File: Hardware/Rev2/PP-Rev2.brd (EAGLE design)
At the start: 190.5 x 101.3 mm, 181 parts, among them IC1 LT6004, IC2 TLC6C5912-Q1, J1 J_0399700102, Q1 MOSFET-PCHANNEL, Q10 2N7002PW, Q11 2N7002PW, Q12 2N7002PW, Q13 2N7002PW, Q14 2N7002PW, Q15 2N7002PW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

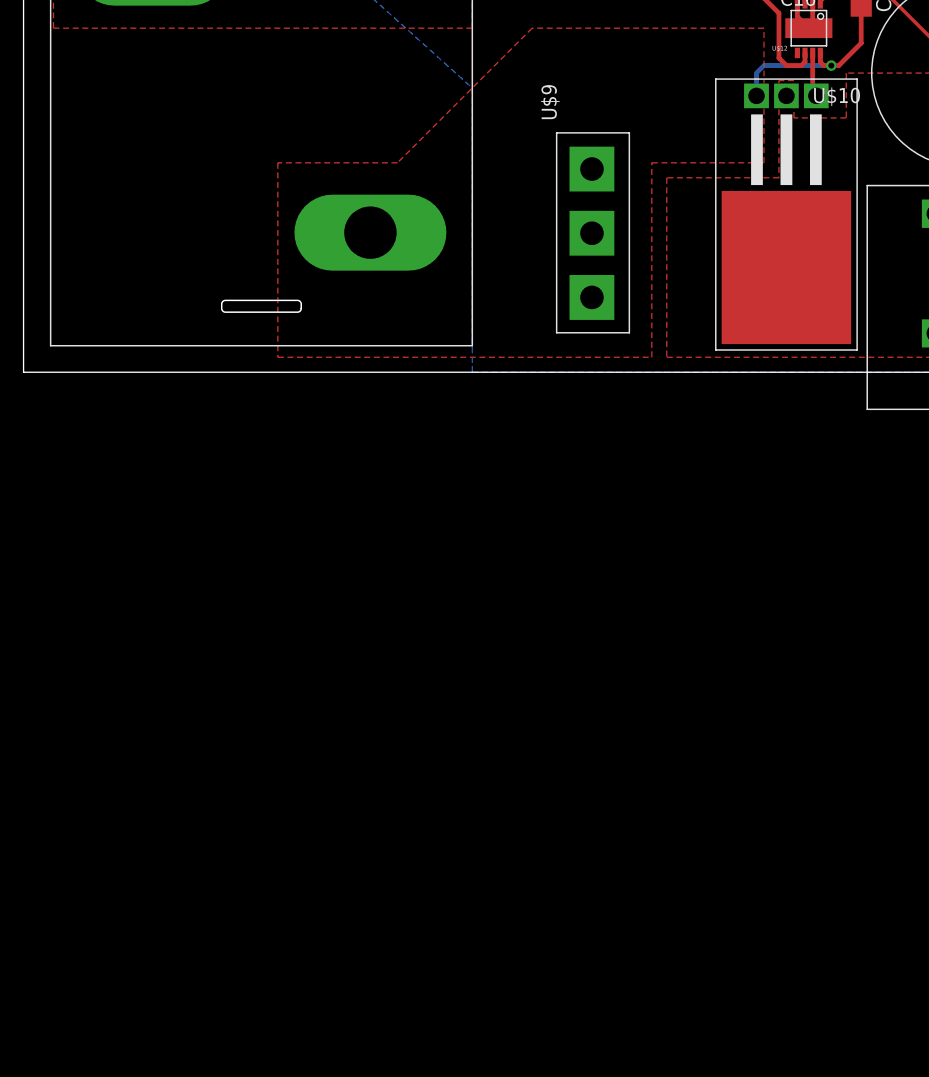
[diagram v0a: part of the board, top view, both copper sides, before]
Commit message: Changing out charger MOSFET to proper component
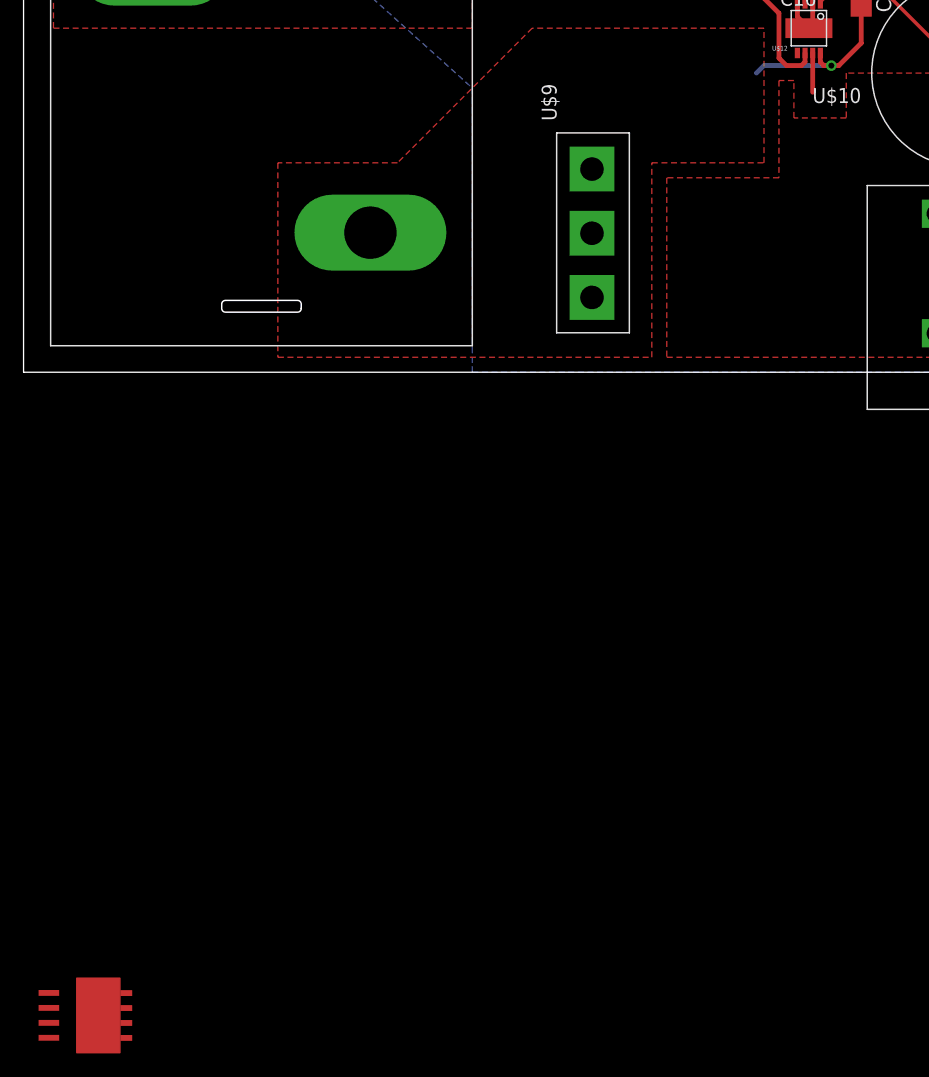
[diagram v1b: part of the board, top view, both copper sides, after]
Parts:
- removed Q9: CSD18532, PCB0M1:TO-220-FLAT
- added U$16: IRFH7191, 2016PowerPackLibraries:PQFN5X6B
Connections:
- net CHARGER+: now also U$16.P$5, U$16.P$6, U$16.P$7, U$16.P$8; no longer Q9.2, Q9.4
- net N$39: now also U$16.P$1, U$16.P$2, U$16.P$3; no longer Q9.3
- net N$40: now also U$16.P$4; no longer Q9.1
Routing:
- net N$39: track 16.8 -> 14.8 mm
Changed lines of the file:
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@@
 <?xml version="1.0" encoding="utf-8"?>
 <!DOCTYPE eagle SYSTEM "eagle.dtd">
-<eagle version="7.1.0">
+<eagle version="6.5.0">
 <drawing>
 <settings>
@@
 <pass name="Default">
 <param name="RoutingGrid" value="50mil"/>
-<param name="AutoGrid" value="1"/>
-<param name="Efforts" value="0"/>
-<param name="TopRouterVariant" value="1"/>
 <param name="tpViaShape" value="round"/>
 <param name="PrefDir.1" value="|"/>
@@
 <element name="U$7" library="MRDT-2015-PowerBoard" package="C_16MM" value="C_108CKH050M" x="11.43" y="54.61"/>
 <element name="U$9" library="2016PowerPackLibraries" package="TO-247-VERT" value="D-STTH60P03SW" x="48.26" y="6.35" rot="R90"/>
-<element name="Q9" library="PCB0M1" package="TO-220-FLAT" value="CSD18532" x="64.77" y="8.89" rot="R180"/>
 <element name="U$10" library="MRDT-2015-PowerBoard" package="C_16MM" value="C_108CKH050M" x="80.01" y="25.4" rot="R180"/>
 <element name="U$11" library="MRDT-2015-PowerBoard" package="C_16MM" value="C_108CKH050M" x="97.79" y="27.305" rot="R180"/>
@@
 <element name="U$15" library="MAX3077" package="MAX3070E" value="MAX3077" x="179.705" y="47.625"/>
 <element name="J1" library="MRDT-2014-All" package="J_2CONHC" value="J_0399700102" x="82.55" y="6.35"/>
+<element name="U$16" library="2016PowerPackLibraries" package="PQFN5X6B" value="IRFH7191" x="6.35" y="-54.61"/>
 </elements>
 <signals>
@@
 </signal>
 <signal name="CHARGER+">
-<contactref element="Q9" pad="4"/>
-<contactref element="Q9" pad="2"/>
 <contactref element="U$10" pad="+"/>
 <contactref element="U$11" pad="+"/>
@@
 <wire x1="100.33" y1="21.59" x2="97.85" y2="21.59" width="0.3048" layer="16"/>
 <wire x1="97.85" y1="21.59" x2="97.79" y2="23.555" width="0.3048" layer="16"/>
+<contactref element="U$16" pad="P$5"/>
+<contactref element="U$16" pad="P$6"/>
+<contactref element="U$16" pad="P$7"/>
+<contactref element="U$16" pad="P$8"/>
+<wire x1="80.01" y1="21.65" x2="97.85" y2="21.59" width="0" layer="19" extent="16-16"/>
+<wire x1="77.47" y1="13.46" x2="80.01" y2="21.65" width="0" layer="19" extent="1-1"/>
+<wire x1="77.47" y1="3.3" x2="77.47" y2="13.46" width="0" layer="19" extent="1-1"/>
+<wire x1="8.725" y1="-52.71" x2="77.47" y2="3.3" width="0" layer="19" extent="1-1"/>
+<wire x1="8.725" y1="-53.98" x2="8.725" y2="-52.71" width="0" layer="19" extent="1-1"/>
+<wire x1="8.725" y1="-55.25" x2="8.725" y2="-53.98" width="0" layer="19" extent="1-1"/>
+<wire x1="8.725" y1="-56.52" x2="8.725" y2="-55.25" width="0" layer="19" extent="1-1"/>
 </signal>
 <signal name="V_CHECK_CHARGER_IN">
@@
 <contactref element="U$5" pad="P$2"/>
 <contactref element="U$9" pad="P$2"/>
-<contactref element="Q9" pad="3"/>
 <polygon width="1.016" layer="1" thermals="no">
 <vertex x="62.865" y="17.78"/>
@@
 <wire x1="68.58" y1="26.035" x2="62.865" y2="26.035" width="0.4064" layer="16"/>
 <wire x1="62.865" y1="26.035" x2="62.23" y2="25.4" width="0.4064" layer="16"/>
-<wire x1="62.23" y1="25.4" x2="62.23" y2="23.46" width="0.4064" layer="16"/>
+<contactref element="U$16" pad="P$1"/>
+<contactref element="U$16" pad="P$2"/>
+<contactref element="U$16" pad="P$3"/>
+<wire x1="48.26" y1="11.8" x2="62.23" y2="25.4" width="0" layer="19" extent="16-16"/>
+<wire x1="29.45" y1="11.85" x2="48.26" y2="11.8" width="0" layer="19" extent="1-1"/>
+<wire x1="2.15" y1="-52.7" x2="29.45" y2="11.85" width="0" layer="19" extent="1-1"/>
+<wire x1="2.15" y1="-53.97" x2="2.15" y2="-52.7" width="0" layer="19" extent="1-1"/>
+<wire x1="2.15" y1="-55.24" x2="2.15" y2="-53.97" width="0" layer="19" extent="1-1"/>
 </signal>
 <signal name="N$40">
 <contactref element="U$12" pad="P$7"/>
-<contactref element="Q9" pad="1"/>
 <wire x1="67" y1="27.1045" x2="67" y2="23.77" width="0.4064" layer="1"/>
-<wire x1="67" y1="23.77" x2="67.31" y2="23.46" width="0.4064" layer="1"/>
+<contactref element="U$16" pad="P$4"/>
+<wire x1="2.15" y1="-56.51" x2="67" y2="23.77" width="0" layer="19" extent="1-1"/>
 </signal>
 <signal name="CHARGER_CTL">

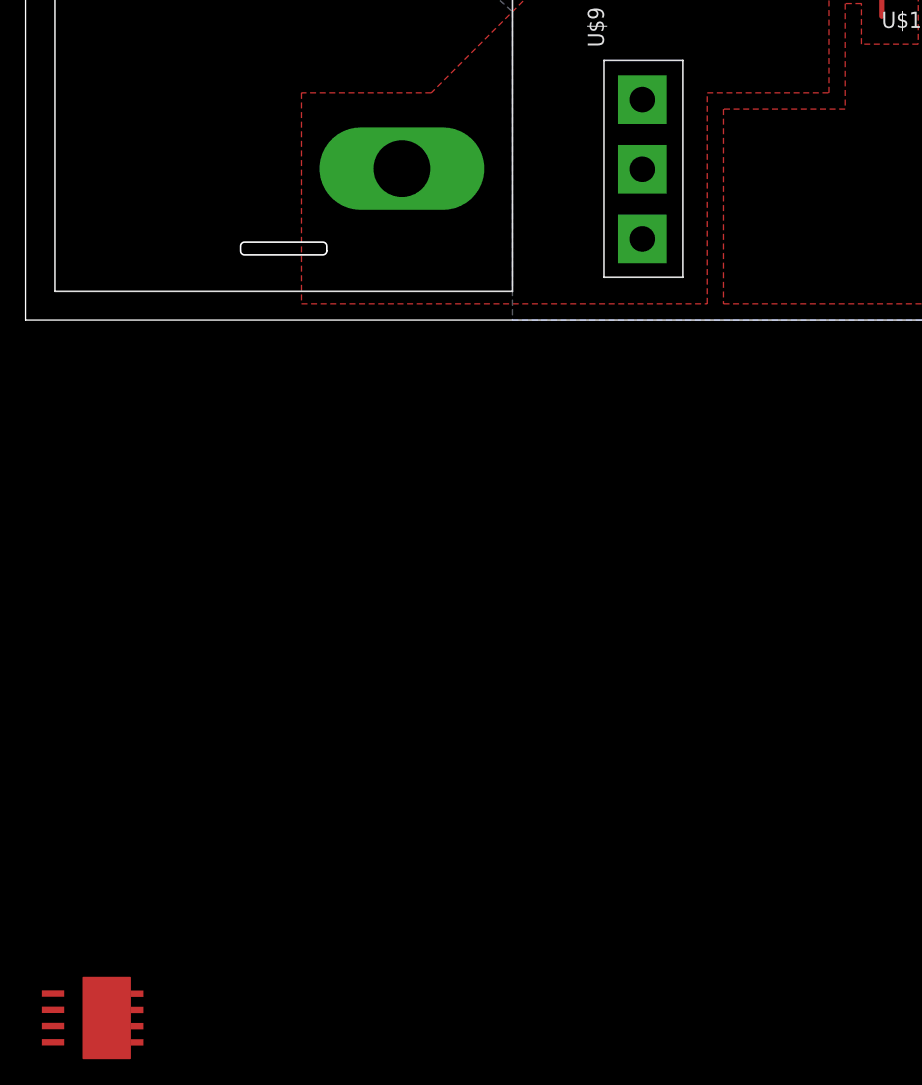
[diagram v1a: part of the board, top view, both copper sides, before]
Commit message: Complete SPICE sim for 90% duty cycle case. Updated Eagle files with proper MOSFET
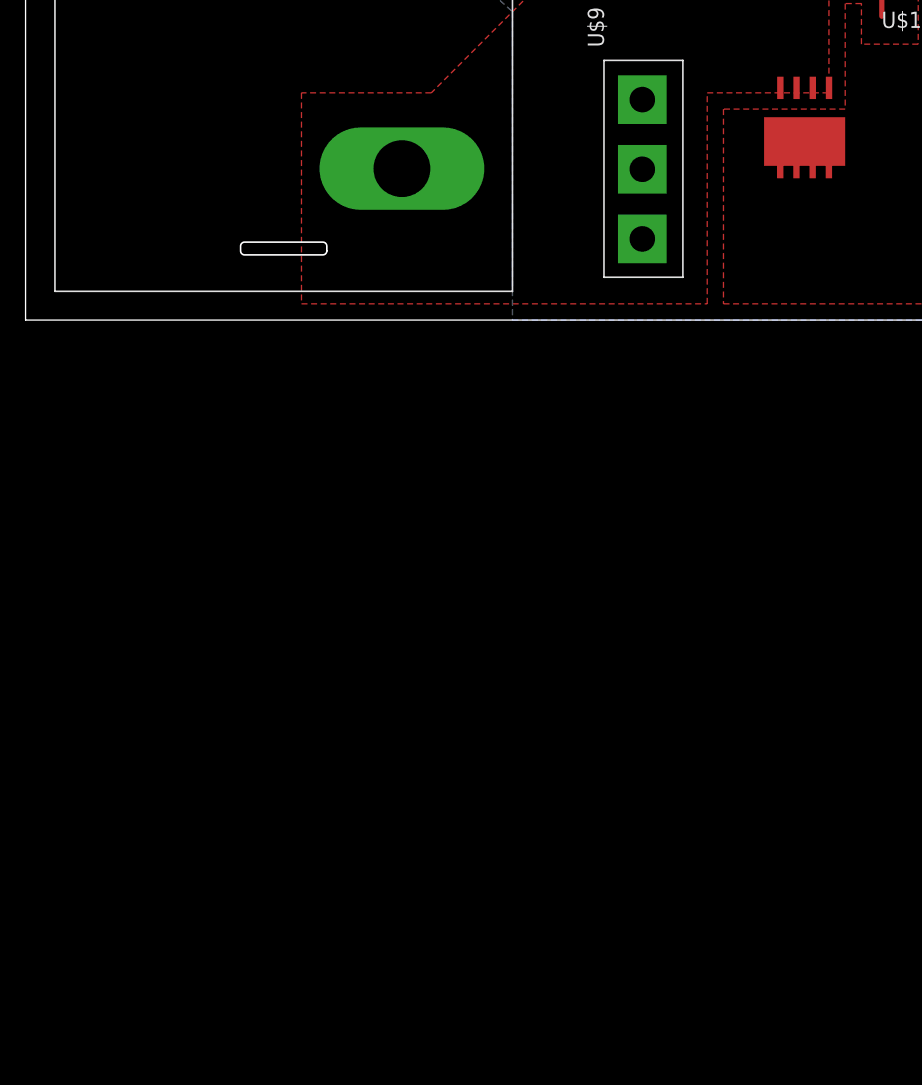
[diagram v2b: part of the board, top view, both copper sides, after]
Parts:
- moved U$16 87.7 mm to (61.0, 14.0), turned to 270 degrees
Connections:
- net CHARGER+: now also U$16.P$9
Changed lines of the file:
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@@
 <element name="U$15" library="MAX3077" package="MAX3070E" value="MAX3077" x="179.705" y="47.625"/>
 <element name="J1" library="MRDT-2014-All" package="J_2CONHC" value="J_0399700102" x="82.55" y="6.35"/>
-<element name="U$16" library="2016PowerPackLibraries" package="PQFN5X6B" value="IRFH7191" x="6.35" y="-54.61"/>
+<element name="U$16" library="2016PowerPackLibraries" package="PQFN5X6B" value="IRFH7191" x="60.96" y="13.97" rot="R270"/>
 </elements>
 <signals>
@@
 <contactref element="U$16" pad="P$7"/>
 <contactref element="U$16" pad="P$8"/>
-<wire x1="80.01" y1="21.65" x2="97.85" y2="21.59" width="0" layer="19" extent="16-16"/>
-<wire x1="77.47" y1="13.46" x2="80.01" y2="21.65" width="0" layer="19" extent="1-1"/>
-<wire x1="77.47" y1="3.3" x2="77.47" y2="13.46" width="0" layer="19" extent="1-1"/>
-<wire x1="8.725" y1="-52.71" x2="77.47" y2="3.3" width="0" layer="19" extent="1-1"/>
-<wire x1="8.725" y1="-53.98" x2="8.725" y2="-52.71" width="0" layer="19" extent="1-1"/>
-<wire x1="8.725" y1="-55.25" x2="8.725" y2="-53.98" width="0" layer="19" extent="1-1"/>
-<wire x1="8.725" y1="-56.52" x2="8.725" y2="-55.25" width="0" layer="19" extent="1-1"/>
+<contactref element="U$16" pad="P$9"/>
 </signal>
 <signal name="V_CHECK_CHARGER_IN">
@@
 <contactref element="U$16" pad="P$2"/>
 <contactref element="U$16" pad="P$3"/>
-<wire x1="48.26" y1="11.8" x2="62.23" y2="25.4" width="0" layer="19" extent="16-16"/>
-<wire x1="29.45" y1="11.85" x2="48.26" y2="11.8" width="0" layer="19" extent="1-1"/>
-<wire x1="2.15" y1="-52.7" x2="29.45" y2="11.85" width="0" layer="19" extent="1-1"/>
-<wire x1="2.15" y1="-53.97" x2="2.15" y2="-52.7" width="0" layer="19" extent="1-1"/>
-<wire x1="2.15" y1="-55.24" x2="2.15" y2="-53.97" width="0" layer="19" extent="1-1"/>
+<wire x1="61.6" y1="18.17" x2="62.23" y2="25.4" width="0" layer="19" extent="1-16"/>
 </signal>
 <signal name="N$40">
@@
 <wire x1="67" y1="27.1045" x2="67" y2="23.77" width="0.4064" layer="1"/>
 <contactref element="U$16" pad="P$4"/>
-<wire x1="2.15" y1="-56.51" x2="67" y2="23.77" width="0" layer="19" extent="1-1"/>
+<wire x1="59.06" y1="18.17" x2="67" y2="23.77" width="0" layer="19" extent="1-1"/>
 </signal>
 <signal name="CHARGER_CTL">

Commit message: Reconfigure board and schematic to include second MOSFET to make synchronous switching possible on the buck converter
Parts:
- removed U$12: LTC4440, 2016PowerPackLibraries:MS8E
- added U$17: IRFH7191, 2016PowerPackLibraries:PQFN5X6B
- added U$18: LTC4444, 2016PowerPackLibraries:MS8E
- moved D20 4.02 mm to (69.8, 33.0), turned to 270 degrees
- moved C16 2.29 mm to (64.8, 31.8)
- moved C15 2.01 mm to (70.5, 30.5), turned to 0 degrees
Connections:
- removed net CHARGER_CTL: U$12.P$1, U$13.8.0
- new net CHARGER_CTL_B: U$13.7.6, U$18.P$2
- new net CHARGER_CTL_T: U$13.8.0, U$18.P$1
- new net N$65: U$17.P$4, U$18.P$4
- net +12V: now also U$18.P$3; no longer U$12.P$3
- net GND: now also U$17.P$1, U$17.P$2, U$17.P$3, U$18.P$9; no longer U$12.P$2, U$12.P$4, U$12.P$9
- net N$38: now also U$18.P$6; no longer U$12.P$6
- net N$39: now also U$17.P$5, U$17.P$6, U$17.P$7, U$17.P$8, U$17.P$9, U$18.P$8; no longer U$12.P$8
- net N$40: now also U$18.P$7; no longer U$12.P$7
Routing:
- net CHARGER_CTL: track 84.0 -> 0.00 mm
- net CHARGER_CTL_T: track 0.00 -> 82.1 mm, vias 0 -> 2
- net CHARGER_CTL_B: track 0.00 -> 80.2 mm, vias 0 -> 3
- net N$38: track 26.7 -> 14.2 mm
- net N$40: track 3.33 -> 15.7 mm
- net N$65: track 0.00 -> 11.5 mm
- net GND: track 746.8 -> 737.9 mm, vias 21 -> 61
- net +12V: track 355.6 -> 361.1 mm
- net N$39: track 14.8 -> 17.4 mm, vias 1 -> 2
- net CHARGER_I_MEAS: track 80.8 -> 83.4 mm
- added copper zone on layer 1, net GND

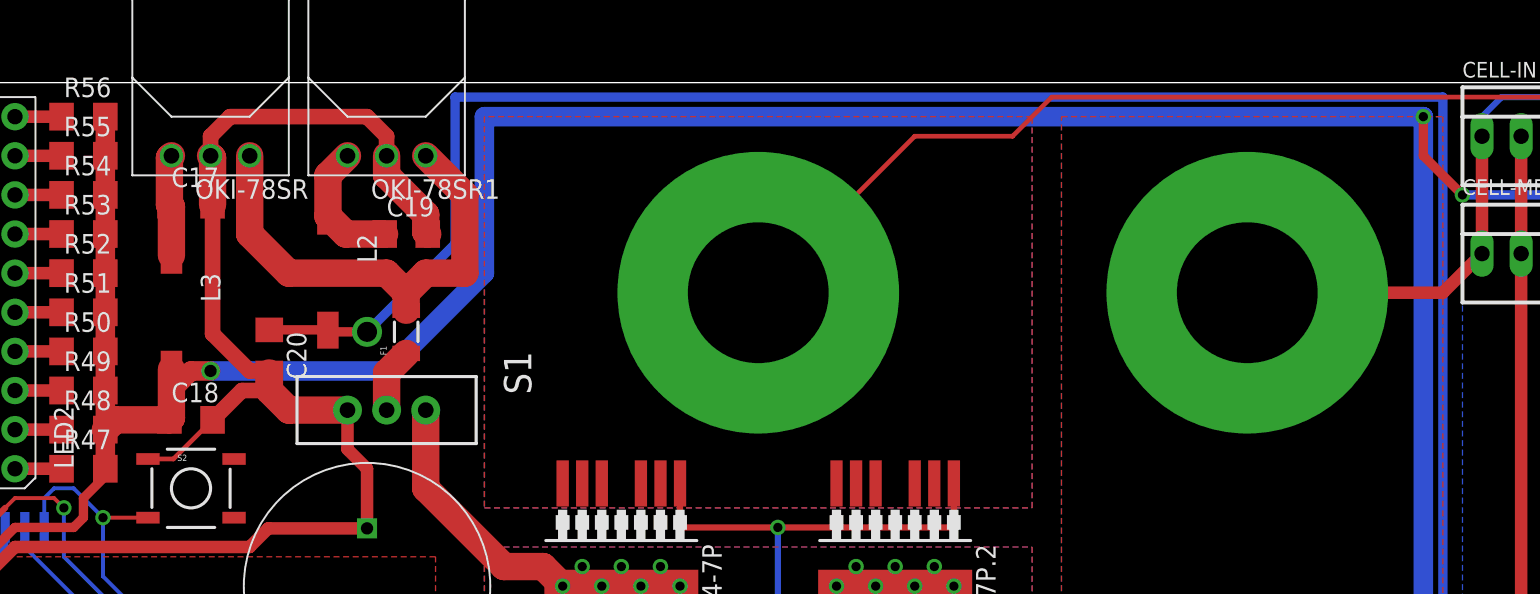
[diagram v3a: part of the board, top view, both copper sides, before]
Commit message: Update board power supply to use proper input/output filtering caps, properly sized PTC fuse on input from battery pack
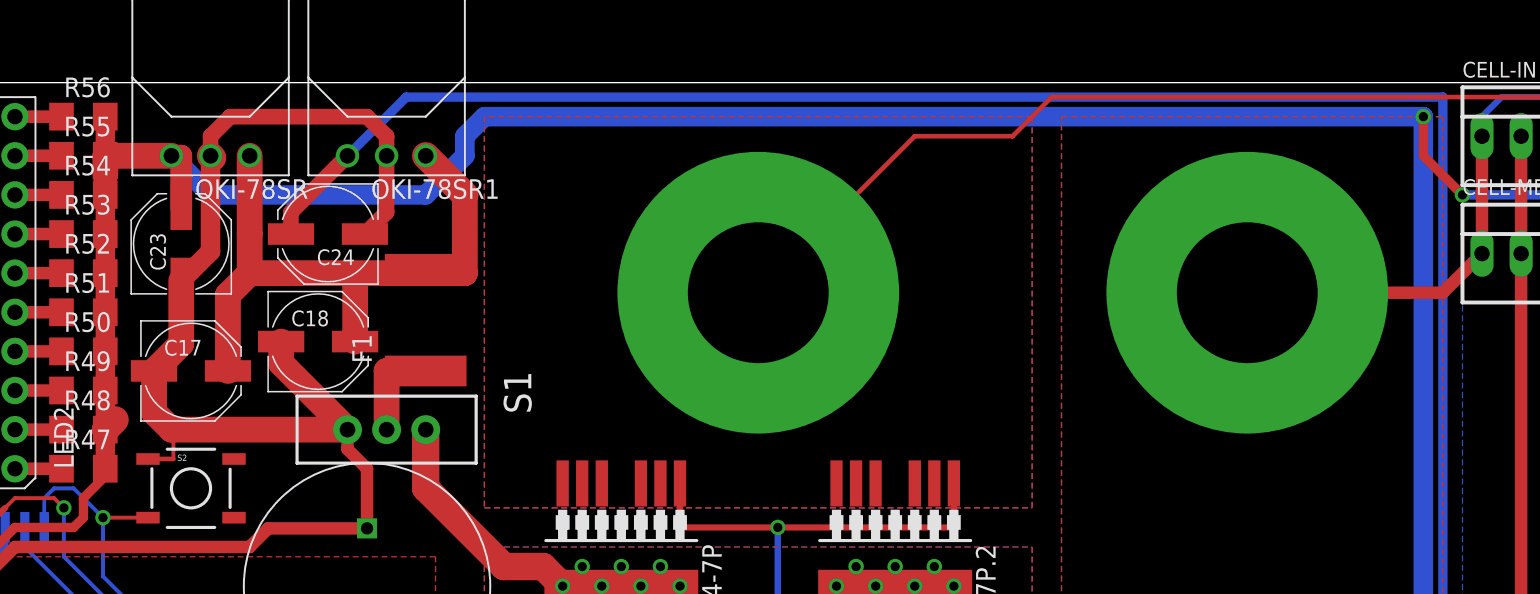
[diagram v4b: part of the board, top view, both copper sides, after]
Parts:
- removed C19, C20: 47µF, resistor:C1206
- removed L2, L3: Fair-Rite 2773019447, rcl:L8530M
- added C23, C24: 22uF, rcl:PANASONIC_D
- C17, C18: value 47µF -> 10uF, 63V; device resistor:C1206 -> rcl:PANASONIC_D
- F1: value PTCSMD -> PTC2920; device SparkFun-PowerIC:PTC-1206 -> 2016PowerPackLibraries:2920
- moved C17 10.8 mm to (33.0, 82.5)
- moved C18 9.69 mm to (41.3, 84.5)
- moved F1 2.84 mm to (48.3, 82.5)
- moved S1 1.27 mm to (45.7, 78.7)
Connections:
- removed net N$100: C17.1, L3.1, OKI-78SR.3
- removed net N$33: C19.1, L2.1, OKI-78SR1.3
- net +12V: now also C24.+, OKI-78SR1.3; no longer C20.1, L2.2
- net 5V: now also C23.+, OKI-78SR.3; no longer C18.1, L3.2
- net GND: now also C17.-, C18.-, C23.-, C24.-; no longer C17.2, C18.2, C19.2, C20.2
- net LOGIC_POWER: now also C17.+, C18.+, F1.P$2; no longer F1.2
- net N$42: now also F1.P$1; no longer F1.1
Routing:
- net LOGIC_POWER: track 31.0 -> 42.1 mm
- net 5V: track 642.8 -> 633.0 mm, vias 19 -> 18
- net +12V: track 361.1 -> 352.3 mm, vias 5 -> 4
- net N$33: track 8.61 -> 0.00 mm
- net GND: track 737.9 -> 745.8 mm
- net N$100: track 6.57 -> 0.00 mm
- net N$42: track 4.21 -> 6.35 mm
- net N$41: track 48.0 -> 46.8 mm
